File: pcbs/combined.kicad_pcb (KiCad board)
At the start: 2 copper layers, 267.6 x 86.8 mm, 94 parts

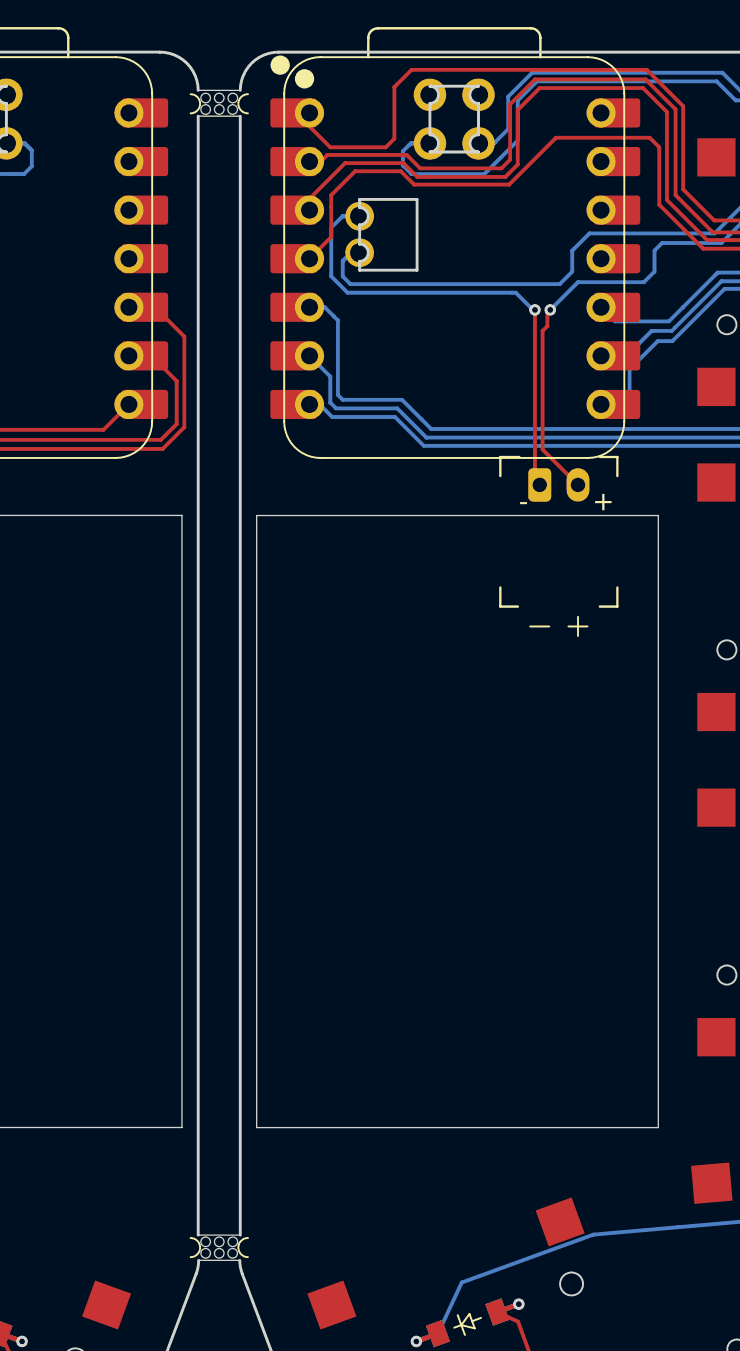
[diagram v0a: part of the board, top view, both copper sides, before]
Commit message: added 2 more mousebite/breakoff points
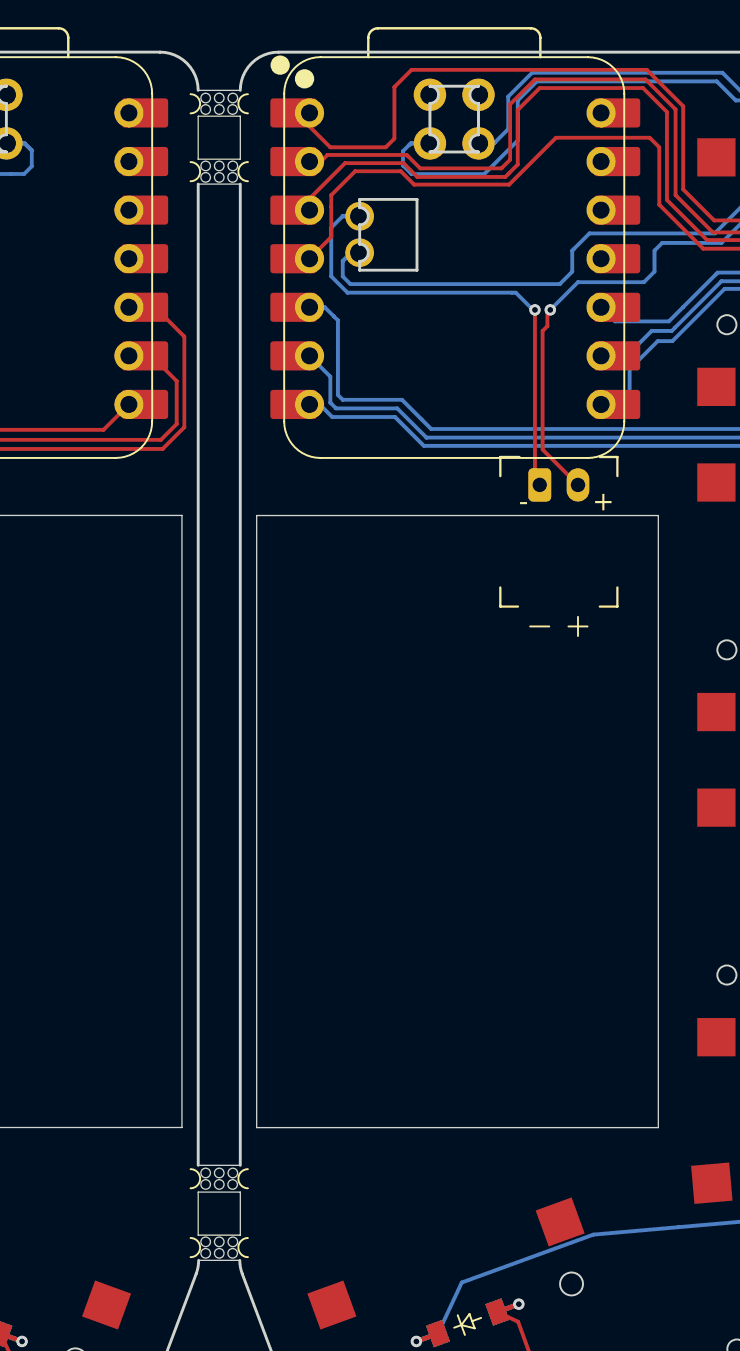
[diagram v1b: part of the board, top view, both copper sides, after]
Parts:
- added mouse-bite-1mm-3mm: VAL**, mouse-bite:mouse-bite-1mm-3mm, F.Cu at (218.5, 44.4)
- added mouse-bite-1mm-3mm: VAL**, mouse-bite:mouse-bite-1mm-3mm, F.Cu at (218.5, 97.0)
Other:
- outline, holes or cut-outs redrawn

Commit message: fix: now correct layers assignment for thru holes (battery and rst) on xiao footprint
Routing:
- net P0: track 300.5 -> 305.1 mm
- net GND: track 249.1 -> 247.9 mm
- net RST: track 207.3 -> 206.2 mm
- net BAT_P: track 120.5 -> 120.0 mm
